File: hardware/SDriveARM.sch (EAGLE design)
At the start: 46 parts, among them IC1 LD117AS33TR, SW1 IS-1290, U1 CY8C4245AXI-483

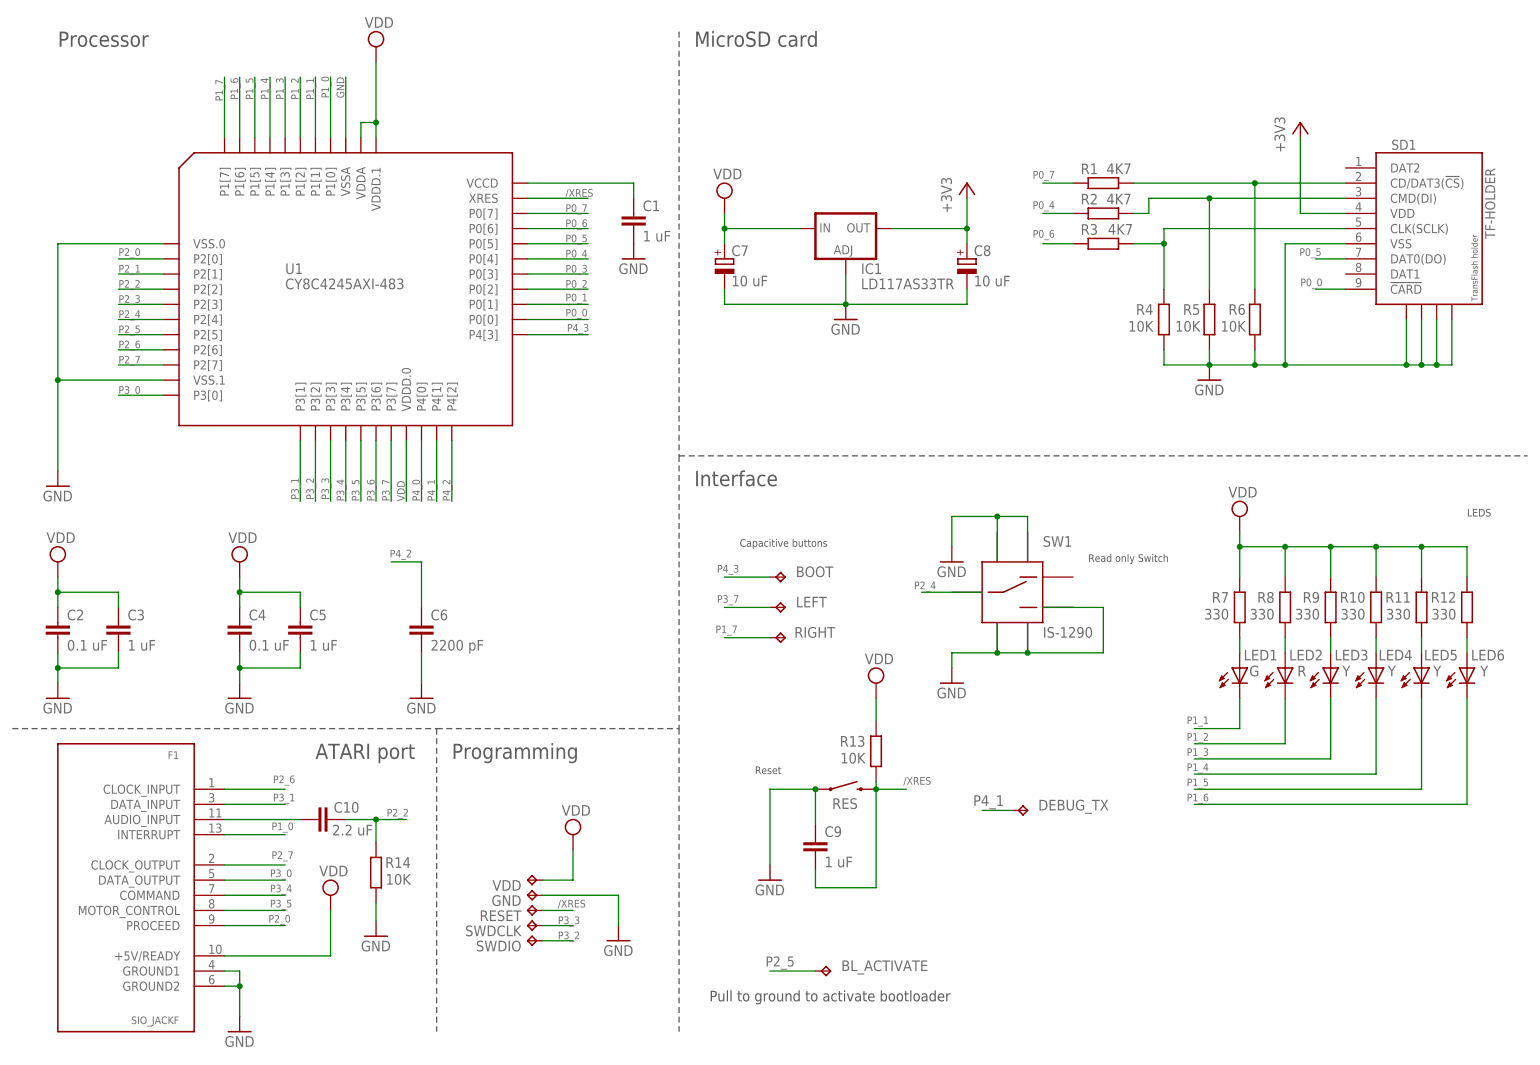
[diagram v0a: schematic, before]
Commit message: Add's documents and photos
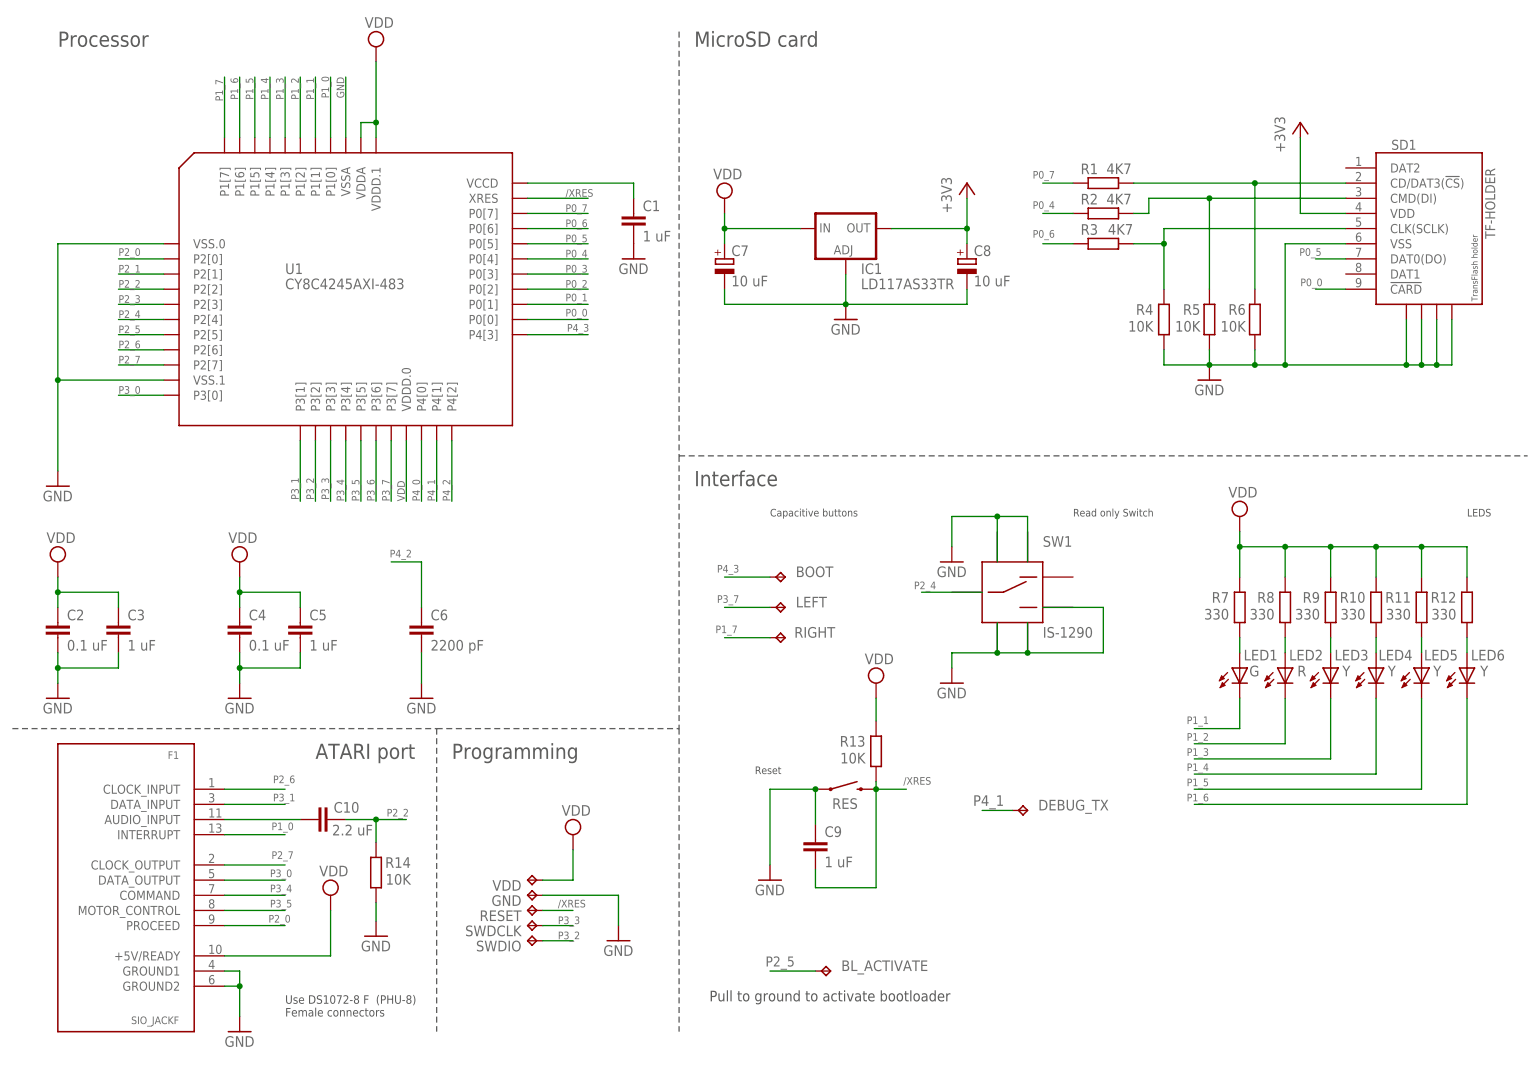
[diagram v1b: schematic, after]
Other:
- note added: "Use DS1072-8 F (PHU-8) Female connectors"
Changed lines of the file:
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@@
 <plain>
 <text x="73.66" y="81.28" size="1.778" layer="98">CMOD Capacitor</text>
-<text x="182.88" y="83.82" size="1.27" layer="97">Read only Switch</text>
-<text x="124.46" y="86.36" size="1.27" layer="97">Capacitive buttons</text>
+<text x="180.34" y="91.44" size="1.27" layer="97">Read only Switch</text>
+<text x="129.54" y="91.44" size="1.27" layer="97">Capacitive buttons</text>
 <wire x1="114.3" y1="172.72" x2="114.3" y2="101.6" width="0.1524" layer="97" style="longdash"/>
 <wire x1="114.3" y1="101.6" x2="114.3" y2="55.88" width="0.1524" layer="97" style="longdash"/>
@@
 <text x="246.38" y="91.44" size="1.27" layer="97">LEDS</text>
 <text x="119.38" y="10.16" size="1.778" layer="97">Pull to ground to activate bootloader</text>
+<text x="48.26" y="7.62" size="1.4224" layer="97">Use DS1072-8 F  (PHU-8)
+Female connectors</text>
 </plain>
 <instances>
@@
 </schematic>
 </drawing>
+<compatibility>
+<note version="6.3" minversion="6.2.2" severity="warning">
+Since Version 6.2.2 text objects can contain more than one line,
+which will not be processed correctly with this version.
+</note>
+</compatibility>
 </eagle>

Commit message: Update HW design to v1.1
Add diode to "SIO data in" to allow work in chain
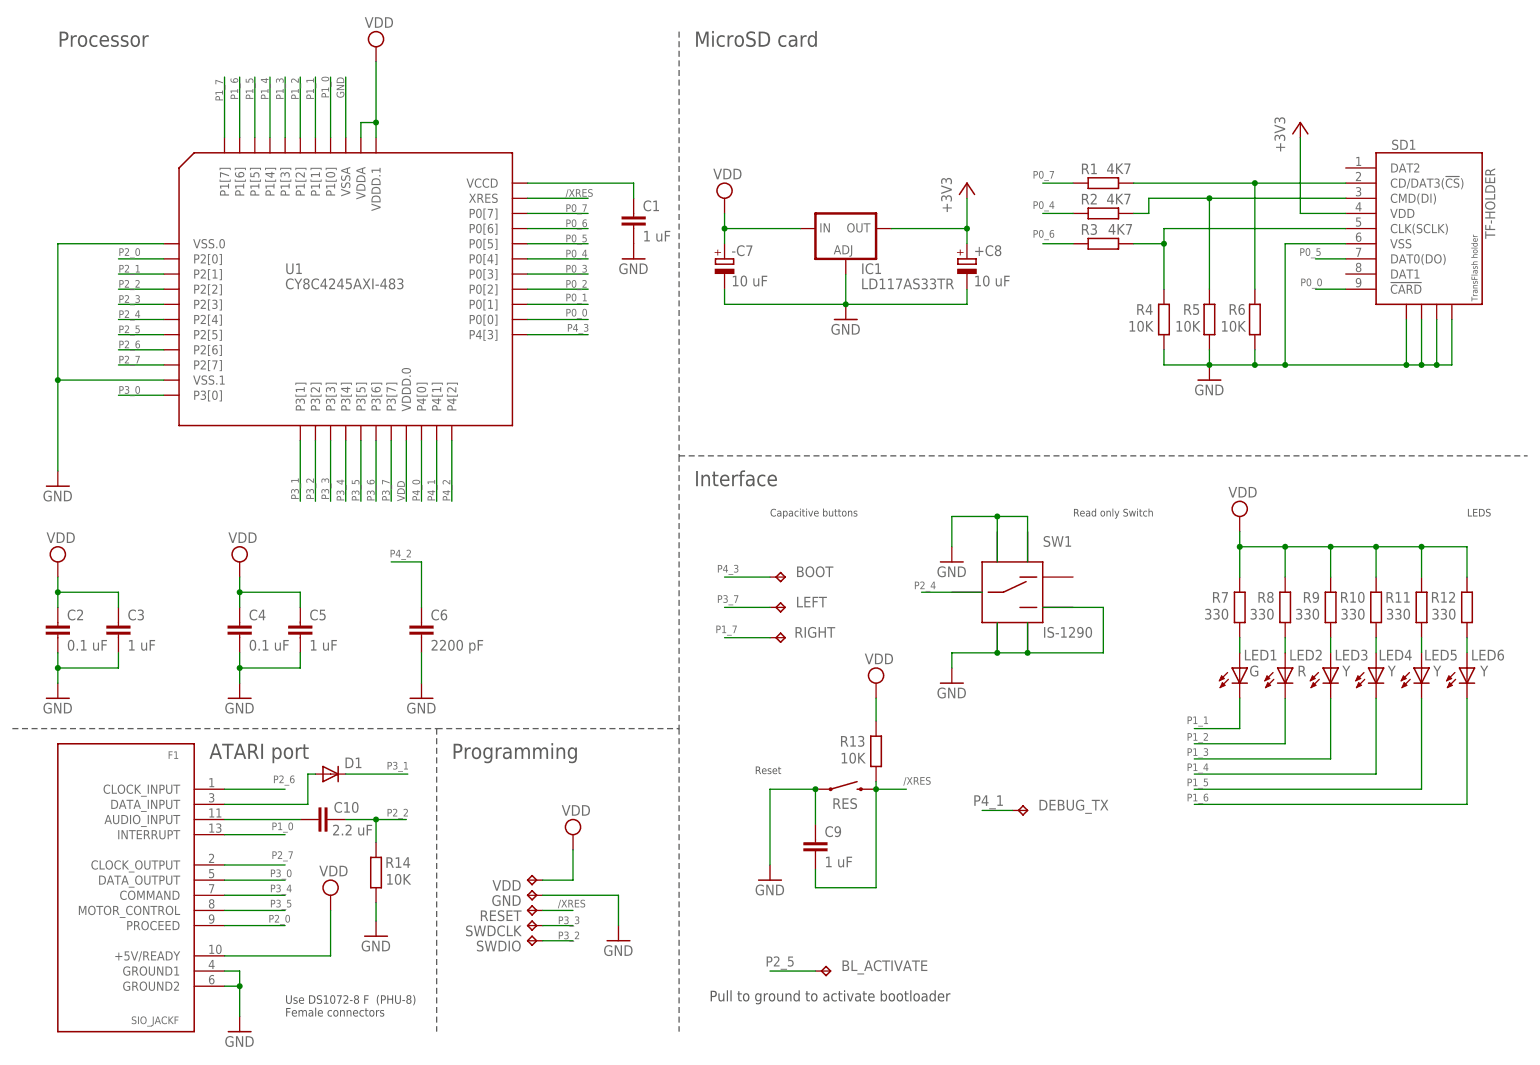
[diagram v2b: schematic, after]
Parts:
- added D1: MBR0520LT, diode:MBR0520LT
- renumbered C7 to -C7, C8 to +C8
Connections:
- new net N$3: D1.A, F1.DATA_INPUT
- net P3_1: now also D1.C; no longer F1.DATA_INPUT
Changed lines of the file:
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@@
 <part name="+3V1" library="supply1" deviceset="+3V3" device=""/>
 <part name="IC1" library="v-reg" deviceset="LD117A?*" device="S" technology="33TR"/>
-<part name="C7" library="resistor" deviceset="CPOL-EU" device="A/3216-18W" value="10 uF"/>
-<part name="C8" library="resistor" deviceset="CPOL-EU" device="A/3216-18W" value="10 uF"/>
+<part name="-C7" library="resistor" deviceset="CPOL-EU" device="A/3216-18W" value="10 uF"/>
+<part name="+C8" library="resistor" deviceset="CPOL-EU" device="A/3216-18W" value="10 uF"/>
 <part name="+3V2" library="supply1" deviceset="+3V3" device=""/>
 <part name="SUPPLY5" library="supply2" deviceset="VDD" device=""/>
@@
 <part name="BL_ACTIVATE" library="testpad" deviceset="TP" device="B1,27" value="TPB1,27"/>
 <part name="DEBUG_TX" library="testpad" deviceset="TP" device="B1,27" value="TPB1,27"/>
+<part name="D1" library="diode" deviceset="MBR0520LT" device=""/>
 </parts>
 <sheets>
@@
 <text x="116.84" y="96.52" size="2.54" layer="97">Interface</text>
 <text x="10.16" y="170.18" size="2.54" layer="97">Processor</text>
-<text x="53.34" y="50.8" size="2.54" layer="97">ATARI port</text>
+<text x="35.56" y="50.8" size="2.54" layer="97">ATARI port</text>
 <text x="127" y="48.26" size="1.27" layer="97">Reset</text>
 <text x="246.38" y="91.44" size="1.27" layer="97">LEDS</text>
@@
 <instance part="+3V1" gate="G$1" x="218.44" y="157.48"/>
 <instance part="IC1" gate="G$1" x="142.24" y="139.7"/>
-<instance part="C7" gate="G$1" x="121.92" y="134.62"/>
-<instance part="C8" gate="G$1" x="162.56" y="134.62"/>
+<instance part="-C7" gate="G$1" x="121.92" y="134.62"/>
+<instance part="+C8" gate="G$1" x="162.56" y="134.62"/>
 <instance part="+3V2" gate="G$1" x="162.56" y="147.32"/>
 <instance part="SUPPLY5" gate="G$1" x="121.92" y="144.78"/>
@@
 <attribute name="NAME" x="174.498" y="42.164" size="1.778" layer="95"/>
 <attribute name="TP_SIGNAL_NAME" x="171.45" y="40.894" size="1.778" layer="97" rot="R270"/>
+</instance>
+<instance part="D1" gate="G$1" x="55.88" y="48.26" smashed="yes">
+<attribute name="NAME" x="58.166" y="49.2506" size="1.778" layer="95"/>
 </instance>
 </instances>
@@
 <wire x1="142.24" y1="132.08" x2="142.24" y2="127" width="0.1524" layer="91"/>
 <pinref part="GND8" gate="1" pin="GND"/>
-<pinref part="C7" gate="G$1" pin="-"/>
+<pinref part="-C7" gate="G$1" pin="-"/>
 <wire x1="121.92" y1="129.54" x2="121.92" y2="127" width="0.1524" layer="91"/>
-<pinref part="C8" gate="G$1" pin="-"/>
+<pinref part="+C8" gate="G$1" pin="-"/>
 <wire x1="162.56" y1="129.54" x2="162.56" y2="127" width="0.1524" layer="91"/>
 <wire x1="121.92" y1="127" x2="142.24" y2="127" width="0.1524" layer="91"/>
@@
 </segment>
 <segment>
-<pinref part="F1" gate="G$$1" pin="DATA_INPUT"/>
-<wire x1="38.1" y1="43.18" x2="48.26" y2="43.18" width="0.1524" layer="91"/>
-<label x="46.228" y="43.688" size="1.27" layer="95"/>
+<pinref part="D1" gate="G$1" pin="C"/>
+<wire x1="58.42" y1="48.26" x2="68.834" y2="48.26" width="0.1524" layer="91"/>
+<label x="65.278" y="49.022" size="1.27" layer="95"/>
 </segment>
 </net>
@@
 <wire x1="134.62" y1="139.7" x2="121.92" y2="139.7" width="0.1524" layer="91"/>
 <wire x1="121.92" y1="139.7" x2="121.92" y2="142.24" width="0.1524" layer="91"/>
-<pinref part="C7" gate="G$1" pin="+"/>
+<pinref part="-C7" gate="G$1" pin="+"/>
 <wire x1="121.92" y1="139.7" x2="121.92" y2="137.16" width="0.1524" layer="91"/>
 <pinref part="SUPPLY5" gate="G$1" pin="VDD"/>
@@
 <wire x1="149.86" y1="139.7" x2="162.56" y2="139.7" width="0.1524" layer="91"/>
 <wire x1="162.56" y1="139.7" x2="162.56" y2="144.78" width="0.1524" layer="91"/>
-<pinref part="C8" gate="G$1" pin="+"/>
+<pinref part="+C8" gate="G$1" pin="+"/>
 <wire x1="162.56" y1="139.7" x2="162.56" y2="137.16" width="0.1524" layer="91"/>
 <pinref part="+3V2" gate="G$1" pin="+3V3"/>
@@
 </segment>
 </net>
+<net name="N$3" class="0">
+<segment>
+<pinref part="F1" gate="G$$1" pin="DATA_INPUT"/>
+<wire x1="38.1" y1="43.18" x2="52.07" y2="43.18" width="0.1524" layer="91"/>
+<wire x1="52.07" y1="43.18" x2="52.07" y2="48.26" width="0.1524" layer="91"/>
+<pinref part="D1" gate="G$1" pin="A"/>
+<wire x1="52.07" y1="48.26" x2="53.34" y2="48.26" width="0.1524" layer="91"/>
+</segment>
+</net>
